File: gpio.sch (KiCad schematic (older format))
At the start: 5 parts, among them J1 CONN_02X20, J2 CONN_02X20, U1 LFE5U-45F-6BG381C

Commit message: schematics: US2 lines for pull with 15k
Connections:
- net labels added: USB_FPGA_PULL_D+, USB_FPGA_PULL_D-
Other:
- note added: "NC v1.7"
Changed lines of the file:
@@
 Text Notes 8350 5200 0    60   ~ 0
 27
+Text GLabel 4200 2200 0    60   Input ~ 0
+USB_FPGA_PULL_D+
+Text GLabel 5700 2200 2    60   Input ~ 0
+USB_FPGA_PULL_D-
+Text Notes 2800 2250 0    60   ~ 0
+NC v1.7
+Text Notes 6750 2250 0    60   ~ 0
+NC v1.7
 $EndSCHEMATC

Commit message: schematics: usb pull pins moved from gpio to gpdi bank gpio is planned to become be voltage changeable 2.5/3.3V while pulls should go to 3.3V
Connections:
- net labels removed: USB_FPGA_PULL_D+, USB_FPGA_PULL_D-
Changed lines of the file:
@@
 Text Notes 8350 5200 0    60   ~ 0
 27
-Text GLabel 4200 2200 0    60   Input ~ 0
-USB_FPGA_PULL_D+
-Text GLabel 5700 2200 2    60   Input ~ 0
-USB_FPGA_PULL_D-
 Text Notes 2800 2250 0    60   ~ 0
 NC v1.7

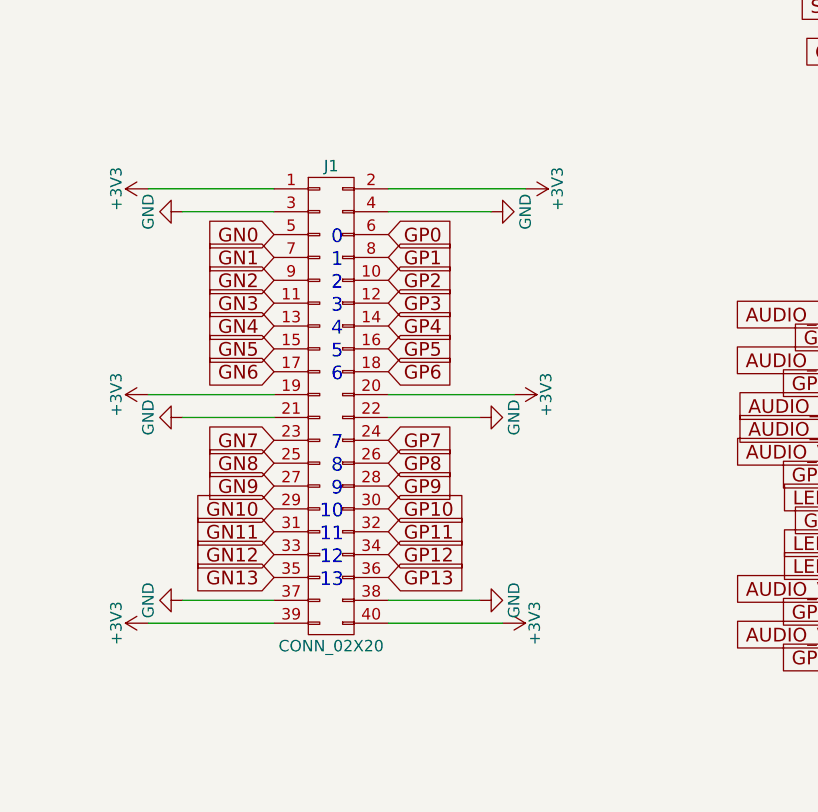
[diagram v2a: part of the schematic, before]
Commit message: schematics: 2V5_3V3 instead fixed 3.3V to J1 connector
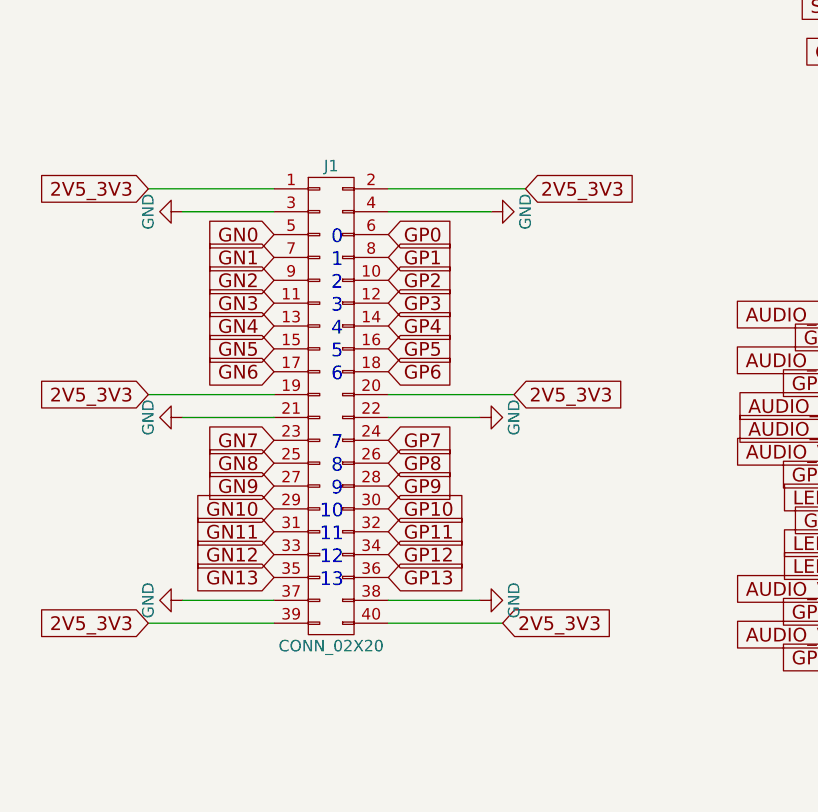
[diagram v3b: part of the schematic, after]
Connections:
- net labels added: 2V5_3V3
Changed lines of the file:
@@
-$EndComp
-$Comp
-L +3V3 #PWR015
-U 1 1 58E6E4F2
-P 1050 5400
-F 0 "#PWR015" H 1050 5250 50  0001 C CNN
-F 1 "+3V3" H 1050 5540 50  0000 C CNN
-F 2 "" H 1050 5400 50  0000 C CNN
-F 3 "" H 1050 5400 50  0000 C CNN
-	1    1050 5400
-	0    -1   -1   0
 $EndComp
 $Comp
@@
 	0    -1   1    0
 $EndComp
-$Comp
-L +3V3 #PWR017
-U 1 1 58E6E53C
-P 2600 5400
-F 0 "#PWR017" H 2600 5250 50  0001 C CNN
-F 1 "+3V3" H 2600 5540 50  0000 C CNN
-F 2 "" H 2600 5400 50  0000 C CNN
-F 3 "" H 2600 5400 50  0000 C CNN
-	1    2600 5400
-	0    1    1    0
-$EndComp
 Wire Wire Line
 	7800 3550 8150 3550
@@
 $EndComp
 $Comp
-L +3V3 #PWR019
-U 1 1 58E710E0
-P 1050 3500
-F 0 "#PWR019" H 1050 3350 50  0001 C CNN
-F 1 "+3V3" H 1050 3640 50  0000 C CNN
-F 2 "" H 1050 3500 50  0000 C CNN
-F 3 "" H 1050 3500 50  0000 C CNN
-	1    1050 3500
-	0    -1   -1   0
-$EndComp
-$Comp
 L GND #PWR020
 U 1 1 58E710E6
@@
 $EndComp
 $Comp
-L +3V3 #PWR021
-U 1 1 58E710EC
-P 1050 4400
-F 0 "#PWR021" H 1050 4250 50  0001 C CNN
-F 1 "+3V3" H 1050 4540 50  0000 C CNN
-F 2 "" H 1050 4400 50  0000 C CNN
-F 3 "" H 1050 4400 50  0000 C CNN
-	1    1050 4400
-	0    -1   -1   0
-$EndComp
-$Comp
 L GND #PWR022
 U 1 1 58E710F2
@@
 $EndComp
 $Comp
-L +3V3 #PWR024
-U 1 1 58E71191
-P 2700 3500
-F 0 "#PWR024" H 2700 3350 50  0001 C CNN
-F 1 "+3V3" H 2700 3640 50  0000 C CNN
-F 2 "" H 2700 3500 50  0000 C CNN
-F 3 "" H 2700 3500 50  0000 C CNN
-	1    2700 3500
-	0    1    1    0
-$EndComp
-$Comp
 L GND #PWR025
 U 1 1 58E71197
@@
 	1    2500 4500
 	0    -1   1    0
-$EndComp
-$Comp
-L +3V3 #PWR026
-U 1 1 58E7119D
-P 2650 4400
-F 0 "#PWR026" H 2650 4250 50  0001 C CNN
-F 1 "+3V3" H 2650 4540 50  0000 C CNN
-F 2 "" H 2650 4400 50  0000 C CNN
-F 3 "" H 2650 4400 50  0000 C CNN
-	1    2650 4400
-	0    1    1    0
 $EndComp
 $Comp
@@
 Text Notes 6750 2250 0    60   ~ 0
 NC v1.7
+Text GLabel 1050 3500 0    60   Input ~ 0
+2V5_3V3
+Text GLabel 1050 4400 0    60   Input ~ 0
+2V5_3V3
+Text GLabel 1050 5400 0    60   Input ~ 0
+2V5_3V3
+Text GLabel 2600 5400 2    60   Input ~ 0
+2V5_3V3
+Text GLabel 2650 4400 2    60   Input ~ 0
+2V5_3V3
+Text GLabel 2700 3500 2    60   Input ~ 0
+2V5_3V3
 $EndSCHEMATC

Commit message: schematics: kicad 5 load and save
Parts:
- D51, D52: symbol D_Schottky_Small -> ulx3s-rescue:D_Schottky_Small
- J1, J2: symbol CONN_02X20 -> micro-hdmi-d:CONN_02X20
- U1: symbol LFE5U-45F-6BG381C -> lfe5bg381:LFE5U-45F-6BG381C
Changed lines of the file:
@@
-EESchema Schematic File Version 2
-LIBS:ulx3s-rescue
-LIBS:power
-LIBS:device
-LIBS:transistors
-LIBS:conn
-LIBS:linear
-LIBS:regul
-LIBS:74xx
-LIBS:cmos4000
-LIBS:adc-dac
-LIBS:memory
-LIBS:xilinx
-LIBS:microcontrollers
-LIBS:dsp
-LIBS:microchip
-LIBS:analog_switches
-LIBS:motorola
-LIBS:texas
-LIBS:intel
-LIBS:audio
-LIBS:interface
-LIBS:digital-audio
-LIBS:philips
-LIBS:display
-LIBS:cypress
-LIBS:siliconi
-LIBS:opto
-LIBS:atmel
-LIBS:contrib
-LIBS:valves
-LIBS:ESP8266
-LIBS:lfe5bg381
-LIBS:micro-hdmi-d
-LIBS:ap3429a
-LIBS:ft2232
-LIBS:ESP32
-LIBS:ssd_13xx
-LIBS:ftdi
-LIBS:max1112x
-LIBS:micro_sd_card_cd
-LIBS:mt48lc16m16a2tg
-LIBS:usb_otg
+EESchema Schematic File Version 4
 LIBS:ulx3s-cache
-EELAYER 25 0
+EELAYER 26 0
 EELAYER END
 $Descr A4 11693 8268
@@
 $EndDescr
 $Comp
-L GND #PWR16
+L power:GND #PWR16
 U 1 1 56AC4825
 P 7800 3550
@@
 $EndComp
 $Comp
-L GND #PWR17
+L power:GND #PWR17
 U 1 1 56AC482D
 P 9000 3550
@@
 $EndComp
 $Comp
-L D_Schottky_Small D51
+L ulx3s-rescue:D_Schottky_Small D51
 U 1 1 56AC483B
 P 7450 5350
@@
 IN5V
 $Comp
-L D_Schottky_Small D52
+L ulx3s-rescue:D_Schottky_Small D52
 U 1 1 56AC4846
 P 9400 5350
@@
 OUT5V
 $Comp
-L +5V #PWR11
+L power:+5V #PWR11
 U 1 1 56AC484F
 P 7350 5350
@@
 $EndComp
 $Comp
-L +3V3 #PWR20
+L power:+3V3 #PWR20
 U 1 1 58D5FBBC
 P 9150 3450
@@
 $EndComp
 $Comp
-L +3V3 #PWR13
+L power:+3V3 #PWR13
 U 1 1 58D5FBF3
 P 7650 3450
@@
 $EndComp
 $Comp
-L CONN_02X20 J2
+L micro-hdmi-d:CONN_02X20 J2
 U 1 1 58E6B7F6
 P 8400 4400
@@
 $EndComp
 $Comp
-L CONN_02X20 J1
+L micro-hdmi-d:CONN_02X20 J1
 U 1 1 58E6B835
 P 1850 4450
@@
 $EndComp
 $Comp
-L GND #PWR14
+L power:GND #PWR14
 U 1 1 58E6D572
 P 7750 4450
@@
 $EndComp
 $Comp
-L +3V3 #PWR12
+L power:+3V3 #PWR12
 U 1 1 58E6D578
 P 7600 4350
@@
 $EndComp
 $Comp
-L GND #PWR18
+L power:GND #PWR18
 U 1 1 58E6D59D
 P 9050 4450
@@
 $EndComp
 $Comp
-L +3V3 #PWR21
+L power:+3V3 #PWR21
 U 1 1 58E6D5A3
 P 9200 4350
@@
 $EndComp
 $Comp
-L GND #PWR15
+L power:GND #PWR15
 U 1 1 58E6E4EC
 P 7750 5250
@@
 $EndComp
 $Comp
-L GND #PWR19
+L power:GND #PWR19
 U 1 1 58E6E536
 P 9050 5250
@@
 	7750 5250 8150 5250
 $Comp
-L GND #PWR5
+L power:GND #PWR5
 U 1 1 58E710CC
 P 1200 3600
@@
 $EndComp
 $Comp
-L GND #PWR6
+L power:GND #PWR6
 U 1 1 58E710E6
 P 1200 4500
@@
 $EndComp
 $Comp
-L GND #PWR7
+L power:GND #PWR7
 U 1 1 58E710F2
 P 1200 5300
@@
 	1200 5300 1600 5300
 $Comp
-L GND #PWR10
+L power:GND #PWR10
 U 1 1 58E7117D
 P 2550 3600
@@
 $EndComp
 $Comp
-L GND #PWR8
+L power:GND #PWR8
 U 1 1 58E71197
 P 2500 4500
@@
 $EndComp
 $Comp
-L GND #PWR9
+L power:GND #PWR9
 U 1 1 58E711A3
 P 2500 5300
@@
 	2100 5300 2500 5300
 $Comp
-L +5V #PWR22
+L power:+5V #PWR22
 U 1 1 58E75077
 P 9500 5350
@@
 AUDIO_V0
 $Comp
-L LFE5U-45F-6BG381C U1
+L lfe5bg381:LFE5U-45F-6BG381C U1
 U 6 1 5A0783C9
 P 4900 4750
@@
 $EndComp
 $Comp
-L LFE5U-45F-6BG381C U1
+L lfe5bg381:LFE5U-45F-6BG381C U1
 U 1 1 5A0737C6
 P 4950 2500

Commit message: schematics: replace 45F chip with 85F
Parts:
- U1: value LFE5U-45F-6BG381C -> LFE5U-85F-6BG381C; symbol lfe5bg381:LFE5U-45F-6BG381C -> lfe5bg381:LFE5U-85F-6BG381C; Distributor1_PN 842-LFE5U45F6BG381C -> 842-LFE5U85F6BG381C; MFG_PN LFE5U-45F-6BG381C -> LFE5U-85F-6BG381C
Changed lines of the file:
@@
 AUDIO_V0
 $Comp
-L lfe5bg381:LFE5U-45F-6BG381C U1
+L lfe5bg381:LFE5U-85F-6BG381C U1
 U 6 1 5A0783C9
 P 4900 4750
@@
 AR Path="/56AC389C/5A0783C9" Ref="U1"  Part="6"
 F 0 "U1" H 4900 5700 60  0000 C CNN
-F 1 "LFE5U-45F-6BG381C" H 4900 5600 60  0000 C CNN
+F 1 "LFE5U-85F-6BG381C" H 4900 5600 60  0000 C CNN
 F 2 "lfe5bg381:BGA-381_pitch0.8mm_dia0.4mm" H 3850 5700 60  0001 C CNN
 F 3 "http://www.latticesemi.com/~/media/LatticeSemi/Documents/DataSheets/ECP5/FPGA-DS-02012.pdf" H 3850 5700 60  0001 C CNN
-F 4 "LFE5U-45F-6BG381C" H 4900 4750 60  0001 C CNN "MFG_PN"
+F 4 "LFE5U-85F-6BG381C" H 4900 4750 60  0001 C CNN "MFG_PN"
 F 5 "www.mouser.com" H 4900 4750 60  0001 C CNN "Distributor1_URL"
-F 6 "842-LFE5U45F6BG381C" H 4900 4750 60  0001 C CNN "Distributor1_PN"
+F 6 "842-LFE5U85F6BG381C" H 4900 4750 60  0001 C CNN "Distributor1_PN"
 	6    4900 4750
 	1    0    0    -1
 $EndComp
 $Comp
-L lfe5bg381:LFE5U-45F-6BG381C U1
+L lfe5bg381:LFE5U-85F-6BG381C U1
 U 1 1 5A0737C6
 P 4950 2500
@@
 AR Path="/56AC389C/5A0737C6" Ref="U1"  Part="1"
 F 0 "U1" H 4950 3450 60  0000 C CNN
-F 1 "LFE5U-45F-6BG381C" H 4950 3350 60  0000 C CNN
+F 1 "LFE5U-85F-6BG381C" H 4950 3350 60  0000 C CNN
 F 2 "lfe5bg381:BGA-381_pitch0.8mm_dia0.4mm" H 3900 3450 60  0001 C CNN
 F 3 "http://www.latticesemi.com/~/media/LatticeSemi/Documents/DataSheets/ECP5/FPGA-DS-02012.pdf" H 3900 3450 60  0001 C CNN
-F 4 "LFE5U-45F-6BG381C" H 4950 2500 60  0001 C CNN "MFG_PN"
+F 4 "LFE5U-85F-6BG381C" H 4950 2500 60  0001 C CNN "MFG_PN"
 F 5 "www.mouser.com" H 4950 2500 60  0001 C CNN "Distributor1_URL"
-F 6 "842-LFE5U45F6BG381C" H 4950 2500 60  0001 C CNN "Distributor1_PN"
+F 6 "842-LFE5U85F6BG381C" H 4950 2500 60  0001 C CNN "Distributor1_PN"
 	1    4950 2500
 	1    0    0    -1

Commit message: schematics: hopefully getting rid of all references to micro-gpdi-d
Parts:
- J1, J2: symbol micro-hdmi-d:CONN_02X20 -> Connector_Generic:Conn_02x20_Odd_Even
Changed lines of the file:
@@
 $EndComp
 $Comp
-L micro-hdmi-d:CONN_02X20 J2
+L Connector_Generic:Conn_02x20_Odd_Even J2
 U 1 1 58E6B7F6
-P 8400 4400
-F 0 "J2" H 8400 5450 50  0000 C CNN
-F 1 "CONN_02X20" H 8400 3350 50  0000 C CNN
-F 2 "Socket_Strips:Socket_Strip_Angled_2x20" H 8400 3450 50  0001 C CNN
-F 3 "" H 8400 3450 50  0000 C CNN
-F 4 "Do not install" H 8400 4400 60  0001 C CNN "Note"
-	1    8400 4400
+P 8350 4350
+F 0 "J2" H 8350 5400 50  0000 C CNN
+F 1 "CONN_02X20" H 8350 3300 50  0000 C CNN
+F 2 "Socket_Strips:Socket_Strip_Angled_2x20" H 8350 3400 50  0001 C CNN
+F 3 "" H 8350 3400 50  0000 C CNN
+F 4 "Do not install" H 8350 4350 60  0001 C CNN "Note"
+	1    8350 4350
 	1    0    0    -1
 $EndComp
 $Comp
-L micro-hdmi-d:CONN_02X20 J1
+L Connector_Generic:Conn_02x20_Odd_Even J1
 U 1 1 58E6B835
-P 1850 4450
-F 0 "J1" H 1850 5500 50  0000 C CNN
-F 1 "CONN_02X20" H 1850 3400 50  0000 C CNN
-F 2 "Socket_Strips:Socket_Strip_Angled_2x20" H 1850 3500 50  0001 C CNN
-F 3 "" H 1850 3500 50  0000 C CNN
-F 4 "Do not install" H 1850 4450 60  0001 C CNN "Note"
-	1    1850 4450
+P 1800 4400
+F 0 "J1" H 1800 5450 50  0000 C CNN
+F 1 "CONN_02X20" H 1800 3350 50  0000 C CNN
+F 2 "Socket_Strips:Socket_Strip_Angled_2x20" H 1800 3450 50  0001 C CNN
+F 3 "" H 1800 3450 50  0000 C CNN
+F 4 "Do not install" H 1800 4400 60  0001 C CNN "Note"
+	1    1800 4400
 	1    0    0    -1
 $EndComp
